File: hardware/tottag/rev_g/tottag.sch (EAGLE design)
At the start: 157 parts, among them J1 MICRO_USB_B_HIROSE_ZX62-B-5PA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, J2 CON_MICRO_SDDM3AT-SF-PEJM5, J3 TC2030-JLINK-NL, J4 TC2030-JLINK-NL, J5 TC2030-JLINK-NL, J7 TC2030-JLINK-NL, T1 HHM1595A1, U1 DW1000, U10 STM32F091CC, U11 AB1815-T3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

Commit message: rev_g: [WIP] routing; some parts off bottom
Mostly a routing checkpoing (26 airwires), but also moved the caps
for the +3v3 -> VDDBAT connection on the DW1000 from back to front.
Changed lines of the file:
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@@
 <setting verticaltext="up"/>
 </settings>
-<grid distance="0.1" unitdist="inch" unit="inch" style="lines" multiple="1" display="yes" altdistance="0.01" altunitdist="inch" altunit="inch"/>
+<grid distance="0.1" unitdist="inch" unit="inch" style="lines" multiple="1" display="no" altdistance="0.01" altunitdist="inch" altunit="inch"/>
 <layers>
 <layer number="1" name="Top" color="4" fill="1" visible="no" active="no"/>

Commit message: rev_g: [WIP] all parts off of the bottom
Major TODOs now just remaining routing:
 - easy airwires up by RTC
 - harder airwires getting from nRF to new SD card location
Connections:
- net N$10 renamed NRF_DECAP3
- net N$2 renamed NRF_DECAP5
- net N$20 renamed NRF_DCC
- net N$6 renamed NRF_DECAP1
- net N$9 renamed NRF_DECAP46
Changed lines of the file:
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@@
 </segment>
 </net>
-<net name="N$6" class="0">
+<net name="NRF_DECAP1" class="0">
 <segment>
 <pinref part="U7" gate="G$1" pin="DEC1"/>
@@
 </segment>
 </net>
-<net name="N$9" class="0">
+<net name="NRF_DECAP46" class="0">
 <segment>
 <pinref part="U7" gate="G$1" pin="DEC4"/>
@@
 </segment>
 </net>
-<net name="N$10" class="0">
+<net name="NRF_DECAP3" class="0">
 <segment>
 <pinref part="U7" gate="G$1" pin="DEC3"/>
@@
 </segment>
 </net>
-<net name="N$20" class="0">
+<net name="NRF_DCC" class="0">
 <segment>
 <pinref part="U7" gate="G$1" pin="DCC"/>
@@
 </segment>
 </net>
-<net name="N$2" class="0">
+<net name="NRF_DECAP5" class="0">
 <segment>
 <pinref part="U7" gate="G$1" pin="DEC5"/>

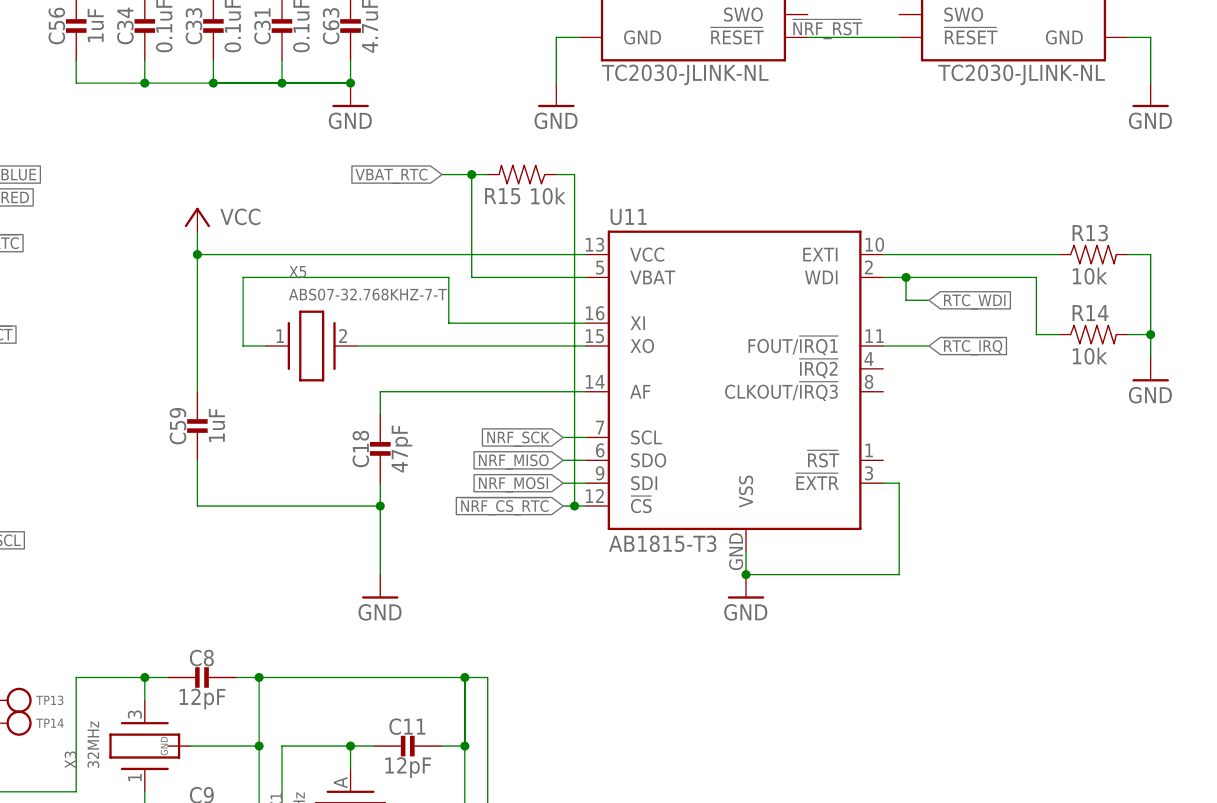
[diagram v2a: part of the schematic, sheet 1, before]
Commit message: rev_g: fix RTC supply to power from +3v3 not VCC
There is no VCC net on tottag :(
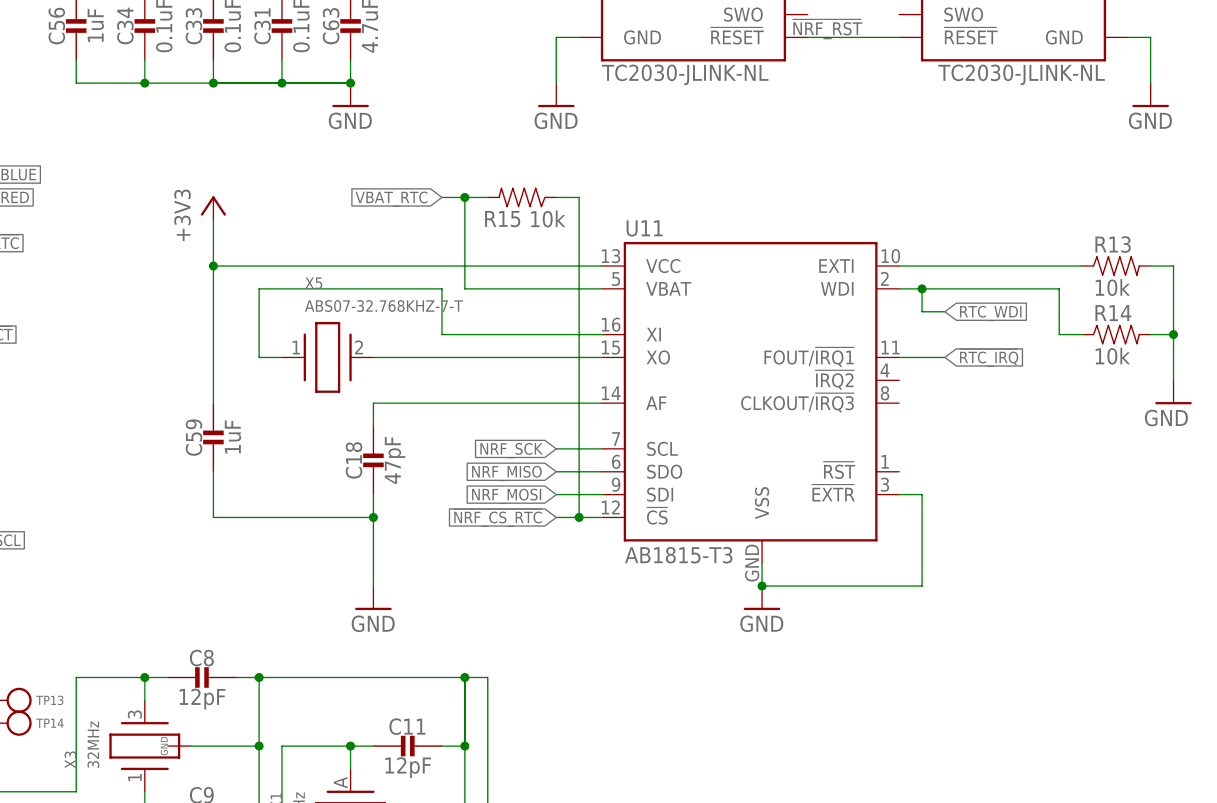
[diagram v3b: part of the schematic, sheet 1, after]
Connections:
- removed net VCC: C59.1, U11.VCC
- net +3V3: now also C59.1, U11.VCC
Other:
- moved on the sheet: C18, C59, R13, R14, R15, U11, X5

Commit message: rev_g: RTC improvements
 - Remove uneeded resistor from EXTI to GND
 - Improve layout of AF cap

The results in renumbering:

R14 : 10k   0402_RES           => R13 : 10k   0402_RES
R15 : 10k   0402_RES           => R14 : 10k   0402_RES

R16 : 11k 1%   0402_RES        => R15 : 11k 1%   0402_RES
R17 : 11k   0402_RES           => R16 : 11k   0402_RES

R18 : 16k   0402_RES           => R17 : 16k   0402_RES

R19 : 100k   0402_RES          => R18 : 100k   0402_RES
R20 : 100k   0402_RES          => R19 : 100k   0402_RES
R21 : 100k   0402_RES          => R20 : 100k   0402_RES
R22 : 100k   0402_RES          => R21 : 100k   0402_RES
R23 : 100k   0402_RES          => R22 : 100k   0402_RES
R24 : 100k   0402_RES          => R23 : 100k   0402_RES

R25 : 2.2M   0402_RES          => R24 : 2.2M   0402_RES

R26 : 10M   0402_RES           => R25 : 10M   0402_RES
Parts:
- removed R26: 10M, passives:RESISTOR0402_RES
- R15: value 10k -> 11k 1%; DIGIKEY 311-10KJRCT-ND -> (none); MPN RC0402JR-0710KL -> (none)
- R16: value 11k 1% -> 11k
- R17: value 11k -> 16k
- R18: value 16k -> 100k
- R24: value 100k -> 2.2M
- R25: value 2.2M -> 10M
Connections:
- removed net N$43: R13.1, U11.EXTI
- net !NRF_CS_RTC: now also R14.1; no longer R15.1
- net !NRF_CS_SD: now also R21.1; no longer R22.1
- net !SD_DETECT: now also R19.1; no longer R20.1
- net BATIN: now also R24.2, R25.1; no longer R25.2, R26.1
- net DW_IRQ: now also R23.2; no longer R24.2
- net GND: now also R15.1, R16.2, R18.2, R23.1, U11.EXTI; no longer R14.2, R16.1, R17.2, R19.2, R25.1
- net N$12: now also R17.2; no longer R18.2
- net N$16: now also R17.1; no longer R18.1
- net N$21: now also R15.2; no longer R16.2
- net N$22: now also R16.1; no longer R17.1
- net N$55: now also R19.2; no longer R23.2
- net NRF_MISO: now also R22.1; no longer R23.1
- net NRF_MOSI: now also R20.1; no longer R21.1
- net RTC_WDI: now also R13.1; no longer R14.1
- net SD_EN: now also R18.1; no longer R19.1
- net VBAT: now also R25.2; no longer R26.2
- net VBAT_RTC: now also R14.2; no longer R15.2
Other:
- moved on the sheet: R13, R14, R16, R17, R19, R20, R21, R22, R25

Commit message: rev_g: update tag-connect part to two side
This is mostly cosmetic, as stacking the two connectors also worked,
but it's really an excuse to learn how the custom 3d part stuff works
with something very easy to model (I just put the pins in for this).
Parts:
- removed J5, J7: TC2030-JLINK-NL, connector:TC2030-JLINK-NL
- J3, J4: value TC2030-JLINK-NL -> TC2030-JLINK-NL-2SIDE; device connector:TC2030-JLINK-NL -> connector:TC2030-JLINK-NL-2SIDE
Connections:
- net !NRF_RST: no longer J4.!RESET
- net !STM_RST: now also J4.!RESET; no longer J5.!RESET, J7.!RESET
- net +3V3: no longer J5.VCC, J7.VCC
- net GND: no longer J5.GND, J7.GND
- net NRF_SWDCLK: no longer J4.SWDCLK
- net NRF_SWDIO: no longer J4.SWDIO
- net STM_SWDCLK: now also J4.SWDCLK; no longer J5.SWDCLK, J7.SWDCLK
- net STM_SWDIO: now also J4.SWDIO; no longer J5.SWDIO, J7.SWDIO
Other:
- moved on the sheet: J3

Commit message: rev_g: documentation fixes
 - Add link in sch to battery test report
 - Delete superfluous `J4` label
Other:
- note added: "Battery testing report https://docs.particle.io/assets/pdfs/electron/battery/IEC62133.pdf"
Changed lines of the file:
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@@
 </text>
 <text x="141.224" y="149.098" size="1.27" layer="98">To nRF ADC</text>
+<text x="99.822" y="171.45" size="0.762" layer="98" align="center-right">Battery testing report
+https://docs.particle.io/assets/pdfs/electron/battery/IEC62133.pdf</text>
 </plain>
 <instances>

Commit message: rev_g: update power plug with 3d model
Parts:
- removed J6: (no value), SparkFun-Connectors:JST_2MM_MALE
- added J5: (no value), connector:JST_2MM_MALE
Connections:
- net GND: now also J5.-; no longer J6.-
- net VBAT: now also J5.+; no longer J6.+
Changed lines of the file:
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@@
 <part name="U4" library="regulators" deviceset="XCL206" device="B"/>
 <part name="GND2" library="supply1" library_urn="urn:adsk.eagle:library:371" deviceset="GND" device=""/>
-<part name="J6" library="SparkFun-Connectors" library_urn="urn:adsk.eagle:library:513" deviceset="JST_2MM_MALE" device="" package3d_urn="urn:adsk.eagle:package:38042/1"/>
 <part name="SUPPLY17" library="regulators" deviceset="GND" device=""/>
 <part name="+3V4" library="regulators" deviceset="+3V3" device=""/>
@@
 <part name="J3" library="connector" library_urn="urn:adsk.eagle:library:20799129" deviceset="TC2030-JLINK" device="-NL-2SIDE" package3d_urn="urn:adsk.eagle:package:20800164/2"/>
 <part name="J4" library="connector" library_urn="urn:adsk.eagle:library:20799129" deviceset="TC2030-JLINK" device="-NL-2SIDE" package3d_urn="urn:adsk.eagle:package:20800164/2"/>
+<part name="J5" library="connector" library_urn="urn:adsk.eagle:library:20799129" deviceset="JST_2MM_MALE" device="" package3d_urn="urn:adsk.eagle:package:20837887/2"/>
 </parts>
 <sheets>
@@
 <attribute name="VALUE" x="230.378" y="158.75" size="1.778" layer="96" rot="R270"/>
 </instance>
-<instance part="J6" gate="G$1" x="109.22" y="177.8" smashed="yes" rot="R90">
-<attribute name="NAME" x="103.378" y="175.26" size="1.778" layer="95" rot="R90"/>
-</instance>
 <instance part="S1" gate="G$1" x="144.78" y="162.56" smashed="yes">
 <attribute name="VALUE" x="142.37" y="157.44" size="1.27" layer="96"/>
 <attribute name="NAME" x="146.92" y="166.67" size="1.27" layer="95" align="bottom-center"/>
+</instance>
+<instance part="J5" gate="G$1" x="109.22" y="177.8" smashed="yes" rot="R90">
+<attribute name="NAME" x="103.378" y="175.26" size="1.778" layer="95" rot="R90"/>
 </instance>
 </instances>
@@
 <wire x1="116.84" y1="172.72" x2="116.84" y2="177.8" width="0.1524" layer="91"/>
 <wire x1="116.84" y1="177.8" x2="114.3" y2="177.8" width="0.1524" layer="91"/>
-<pinref part="J6" gate="G$1" pin="-"/>
+<pinref part="J5" gate="G$1" pin="-"/>
 </segment>
 <segment>
@@
 <junction x="116.84" y="162.56"/>
 <label x="114.554" y="180.594" size="1.778" layer="95"/>
-<pinref part="J6" gate="G$1" pin="+"/>
 <wire x1="114.3" y1="180.34" x2="121.92" y2="180.34" width="0.1524" layer="91"/>
 <wire x1="121.92" y1="180.34" x2="121.92" y2="162.56" width="0.1524" layer="91"/>
@@
 <wire x1="139.7" y1="162.56" x2="129.54" y2="162.56" width="0.1524" layer="91"/>
 <junction x="129.54" y="162.56"/>
-</segment>
-</net>
+<pinref part="J5" gate="G$1" pin="+"/>
+</segment>
+</net>

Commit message: rev_g: replace SD with part with 3d model
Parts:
- J2: value CON_MICRO_SDDM3AT-SF-PEJM5 -> DM3AT-SF-PEJM5; device connector:CON_MICRO_SDDM3AT-SF-PEJM5 -> connector:DM3AT-SF-PEJM5
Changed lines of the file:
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@@
 </part>
 <part name="GND18" library="umich" deviceset="GND" device=""/>
-<part name="J2" library="connector" deviceset="CON_MICRO_SD" device="DM3AT-SF-PEJM5"/>
+<part name="J2" library="connector" library_urn="urn:adsk.eagle:library:20799129" deviceset="DM3AT-SF-PEJM5" device="" package3d_urn="urn:adsk.eagle:package:20799216/2"/>
 <part name="P+10" library="regulators" deviceset="+3V3" device=""/>
 <part name="U8" library="chips" deviceset="SIP32510" device=""/>
